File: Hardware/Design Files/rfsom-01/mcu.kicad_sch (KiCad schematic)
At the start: 10 parts

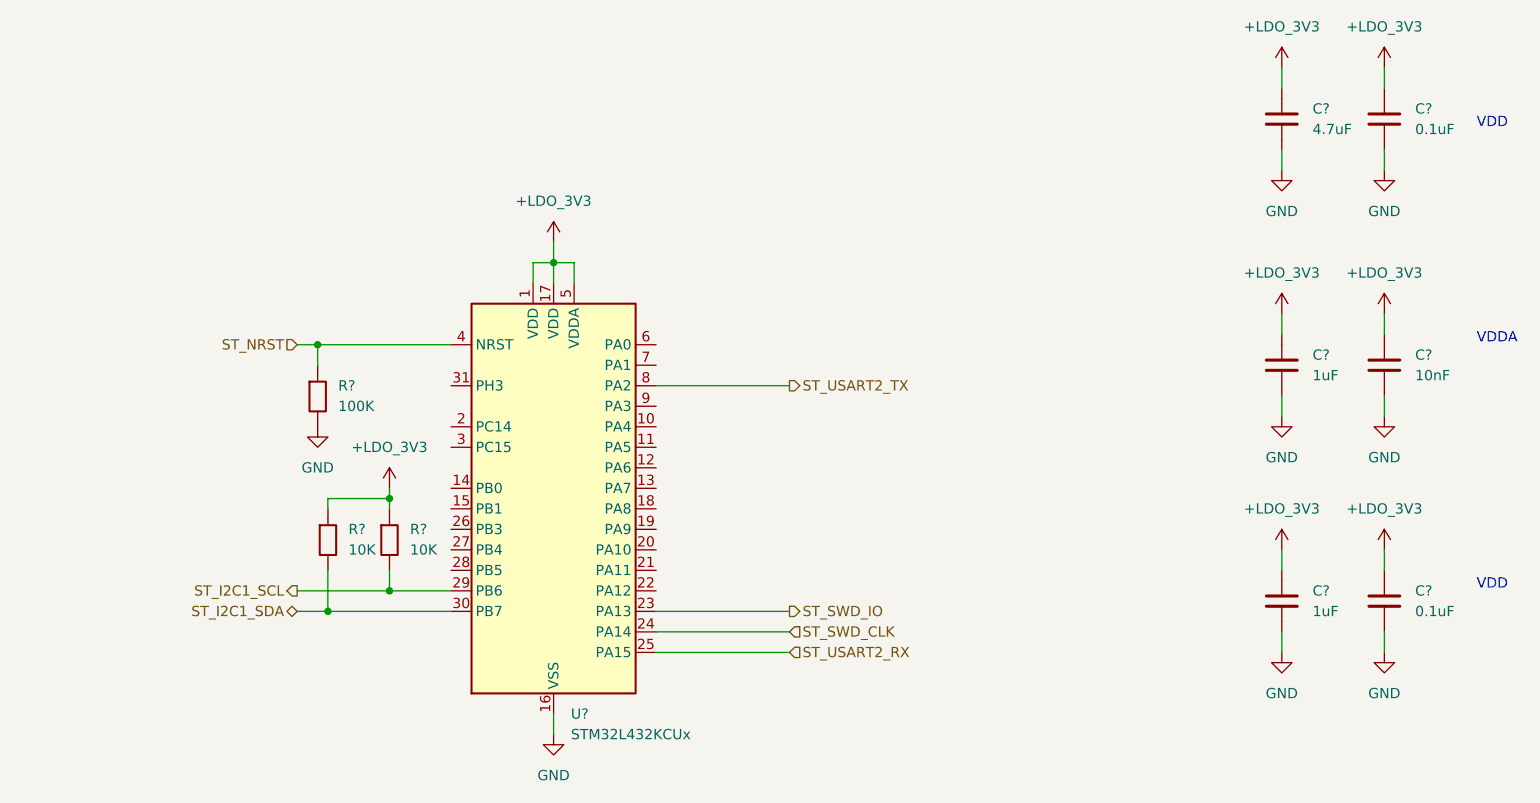
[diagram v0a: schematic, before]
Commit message: ddr progress; added more conns;
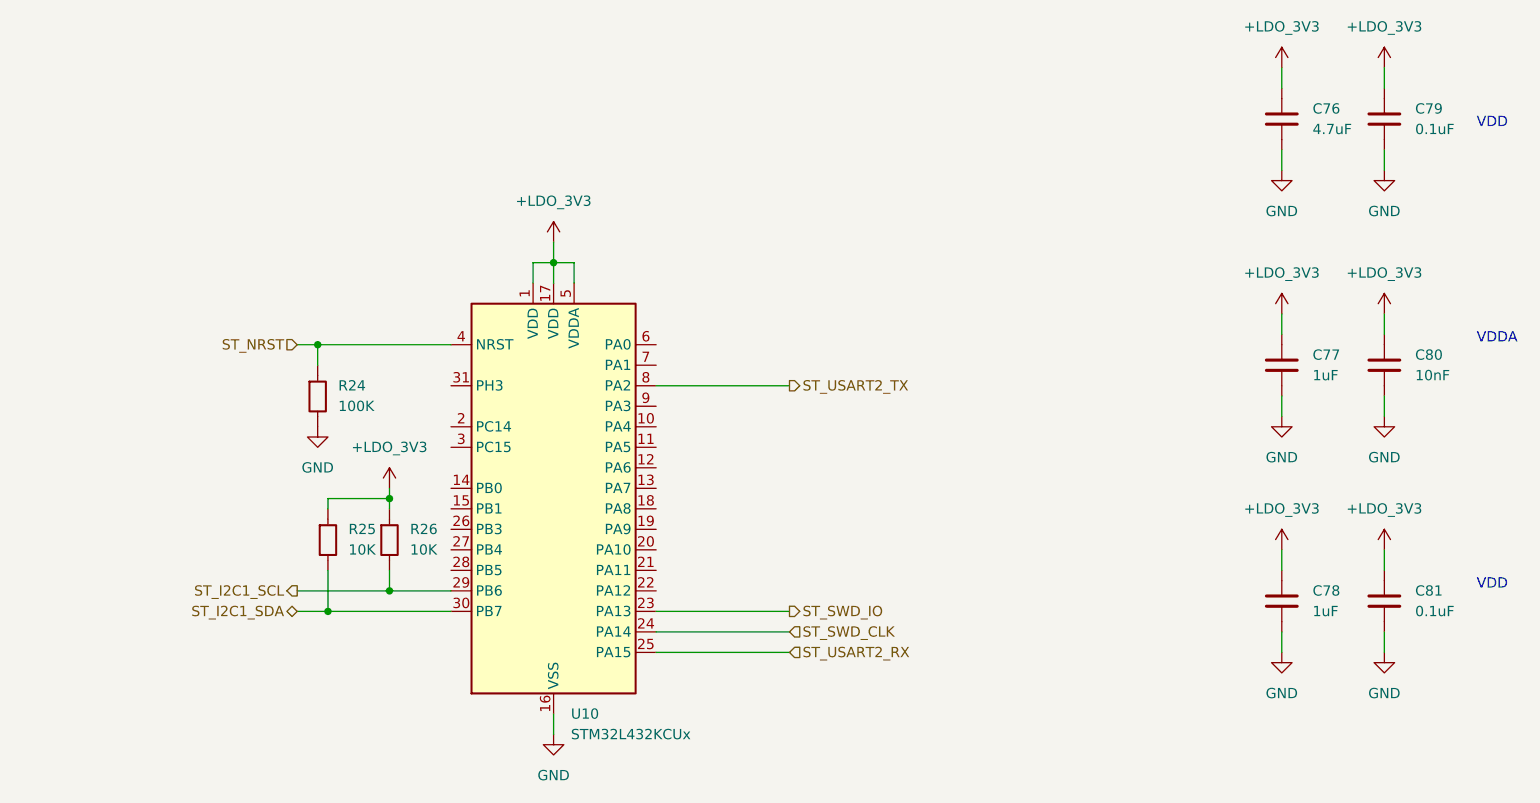
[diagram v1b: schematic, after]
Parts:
- gave numbers to parts that had none: 10
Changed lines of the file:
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@@
 		(dnp no)
 		(fields_autoplaced yes)
-		(property "Reference" "C?"
+		(property "Reference" "C81"
 			(at 240.03 116.8399 0)
 			(effects
@@
 			(project ""
 				(path "/5dade83d-850c-4336-8f49-e0e8e6ebca37/b5d2488c-4141-40ec-97d6-0b993b0cde28"
-					(reference "C?")
+					(reference "C81")
 					(unit 1)
 				)
@@
 		(dnp no)
 		(fields_autoplaced yes)
-		(property "Reference" "C?"
+		(property "Reference" "C79"
 			(at 240.03 57.1499 0)
 			(effects
@@
 			(project "rfsom-01"
 				(path "/5dade83d-850c-4336-8f49-e0e8e6ebca37/b5d2488c-4141-40ec-97d6-0b993b0cde28"
-					(reference "C?")
+					(reference "C79")
 					(unit 1)
 				)
@@
 		(dnp no)
 		(fields_autoplaced yes)
-		(property "Reference" "R?"
+		(property "Reference" "R26"
 			(at 115.57 109.2199 0)
 			(effects
@@
 			(project ""
 				(path "/5dade83d-850c-4336-8f49-e0e8e6ebca37/b5d2488c-4141-40ec-97d6-0b993b0cde28"
-					(reference "R?")
+					(reference "R26")
 					(unit 1)
 				)
@@
 		(dnp no)
 		(fields_autoplaced yes)
-		(property "Reference" "R?"
+		(property "Reference" "R25"
 			(at 107.95 109.2199 0)
 			(effects
@@
 			(project "rfsom-01"
 				(path "/5dade83d-850c-4336-8f49-e0e8e6ebca37/b5d2488c-4141-40ec-97d6-0b993b0cde28"
-					(reference "R?")
+					(reference "R25")
 					(unit 1)
 				)
@@
 		(dnp no)
 		(fields_autoplaced yes)
-		(property "Reference" "R?"
+		(property "Reference" "R24"
 			(at 106.68 91.4399 0)
 			(effects
@@
 			(project ""
 				(path "/5dade83d-850c-4336-8f49-e0e8e6ebca37/b5d2488c-4141-40ec-97d6-0b993b0cde28"
-					(reference "R?")
+					(reference "R24")
 					(unit 1)
 				)
@@
 		(dnp no)
 		(fields_autoplaced yes)
-		(property "Reference" "U?"
+		(property "Reference" "U10"
 			(at 135.4933 132.08 0)
 			(effects
@@
 			(project ""
 				(path "/5dade83d-850c-4336-8f49-e0e8e6ebca37/b5d2488c-4141-40ec-97d6-0b993b0cde28"
-					(reference "U?")
+					(reference "U10")
 					(unit 1)
 				)
@@
 		(dnp no)
 		(fields_autoplaced yes)
-		(property "Reference" "C?"
+		(property "Reference" "C77"
 			(at 227.33 87.6299 0)
 			(effects
@@
 			(project "rfsom-01"
 				(path "/5dade83d-850c-4336-8f49-e0e8e6ebca37/b5d2488c-4141-40ec-97d6-0b993b0cde28"
-					(reference "C?")
+					(reference "C77")
 					(unit 1)
 				)
@@
 		(dnp no)
 		(fields_autoplaced yes)
-		(property "Reference" "C?"
+		(property "Reference" "C78"
 			(at 227.33 116.8399 0)
 			(effects
@@
 			(project ""
 				(path "/5dade83d-850c-4336-8f49-e0e8e6ebca37/b5d2488c-4141-40ec-97d6-0b993b0cde28"
-					(reference "C?")
+					(reference "C78")
 					(unit 1)
 				)
@@
 		(dnp no)
 		(fields_autoplaced yes)
-		(property "Reference" "C?"
+		(property "Reference" "C76"
 			(at 227.33 57.1499 0)
 			(effects
@@
 			(project ""
 				(path "/5dade83d-850c-4336-8f49-e0e8e6ebca37/b5d2488c-4141-40ec-97d6-0b993b0cde28"
-					(reference "C?")
+					(reference "C76")
 					(unit 1)
 				)
@@
 		(dnp no)
 		(fields_autoplaced yes)
-		(property "Reference" "C?"
+		(property "Reference" "C80"
 			(at 240.03 87.6299 0)
 			(effects
@@
 			(project ""
 				(path "/5dade83d-850c-4336-8f49-e0e8e6ebca37/b5d2488c-4141-40ec-97d6-0b993b0cde28"
-					(reference "C?")
-					(unit 1)
-				)
+					(reference "C80")
+					(unit 1)
+				)

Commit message: some ddr routing progress; layerstack per pcbway standard options, review reqd; commit prior to ddr split;
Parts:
- C77, C78: footprint Capacitor_SMD:C_0603_1608Metric_Pad1.08x0.95mm_HandSolder -> Capacitor_SMD:C_0603_1608Metric
- C79, C81: footprint Capacitor_SMD:C_0402_1005Metric_Pad0.74x0.62mm_HandSolder -> Capacitor_SMD:C_0402_1005Metric
- R24: footprint Resistor_SMD:R_0402_1005Metric_Pad0.72x0.64mm_HandSolder -> Resistor_SMD:R_0402_1005Metric
- R25, R26: footprint Resistor_SMD:R_0603_1608Metric_Pad0.98x0.95mm_HandSolder -> Resistor_SMD:R_0603_1608Metric
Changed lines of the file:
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@@
 			)
 		)
-		(property "Footprint" "Capacitor_SMD:C_0402_1005Metric_Pad0.74x0.62mm_HandSolder"
+		(property "Footprint" "Capacitor_SMD:C_0402_1005Metric"
 			(at 236.22 111.76 0)
 			(effects
@@
 			)
 		)
-		(property "Footprint" "Capacitor_SMD:C_0402_1005Metric_Pad0.74x0.62mm_HandSolder"
+		(property "Footprint" "Capacitor_SMD:C_0402_1005Metric"
 			(at 236.22 52.07 0)
 			(effects
@@
 			)
 		)
-		(property "Footprint" "Resistor_SMD:R_0603_1608Metric_Pad0.98x0.95mm_HandSolder"
+		(property "Footprint" "Resistor_SMD:R_0603_1608Metric"
 			(at 113.03 104.14 0)
 			(effects
@@
 			)
 		)
-		(property "Footprint" "Resistor_SMD:R_0603_1608Metric_Pad0.98x0.95mm_HandSolder"
+		(property "Footprint" "Resistor_SMD:R_0603_1608Metric"
 			(at 105.41 104.14 0)
 			(effects
@@
 			)
 		)
-		(property "Footprint" "Resistor_SMD:R_0402_1005Metric_Pad0.72x0.64mm_HandSolder"
+		(property "Footprint" "Resistor_SMD:R_0402_1005Metric"
 			(at 104.14 86.36 0)
 			(effects
@@
 			)
 		)
-		(property "Footprint" "Capacitor_SMD:C_0603_1608Metric_Pad1.08x0.95mm_HandSolder"
+		(property "Footprint" "Capacitor_SMD:C_0603_1608Metric"
 			(at 223.52 82.55 0)
 			(effects
@@
 			)
 		)
-		(property "Footprint" "Capacitor_SMD:C_0603_1608Metric_Pad1.08x0.95mm_HandSolder"
+		(property "Footprint" "Capacitor_SMD:C_0603_1608Metric"
 			(at 223.52 111.76 0)
 			(effects

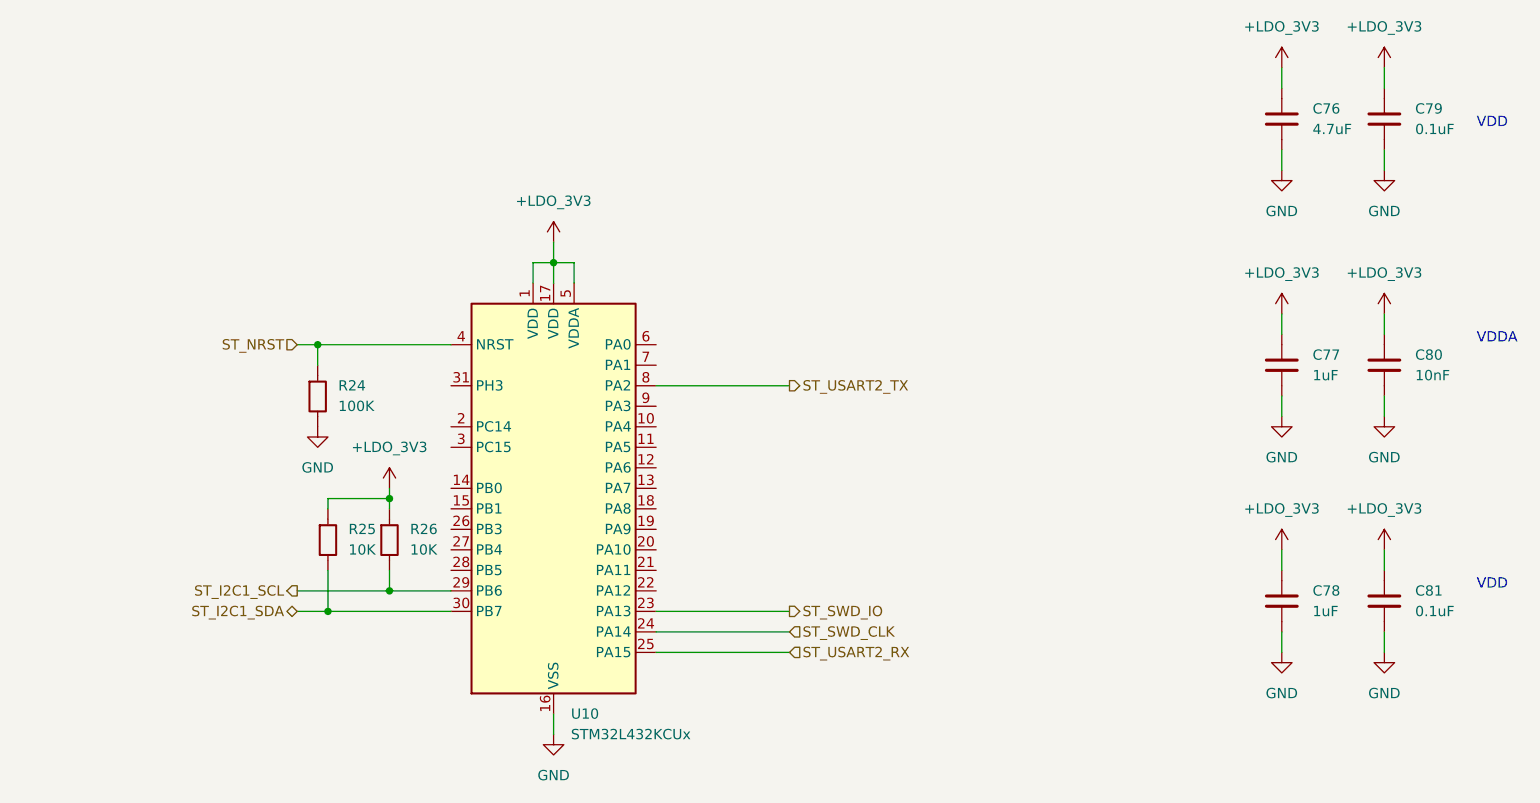
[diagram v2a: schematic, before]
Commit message: replaced pmic;
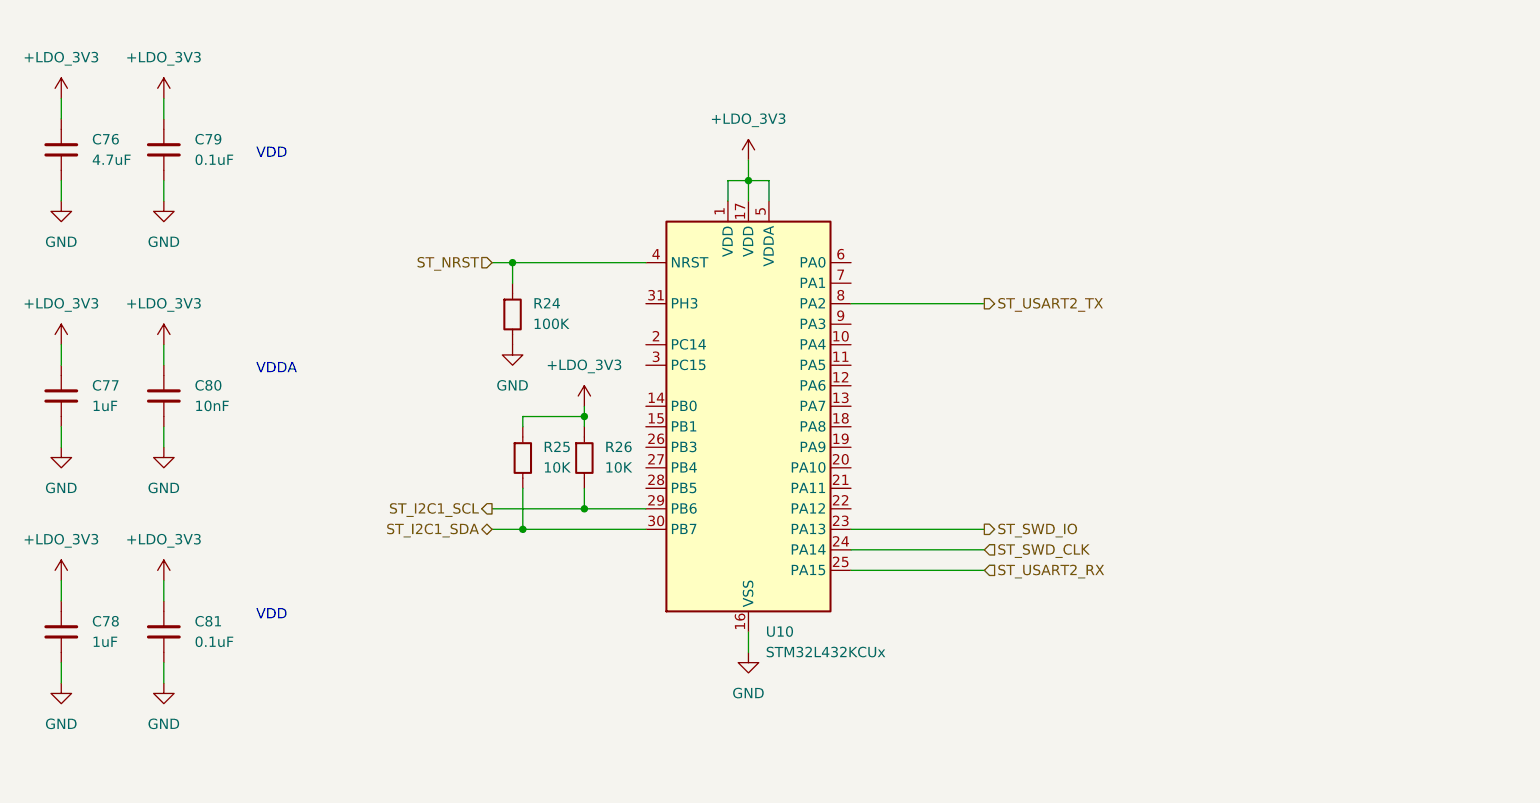
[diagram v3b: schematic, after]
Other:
- moved on the sheet: C76, C77, C78, C79, C80, C81, R24, R25, R26, U10
